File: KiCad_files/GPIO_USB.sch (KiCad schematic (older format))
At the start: 29 parts, among them J9 Conn_02x08_Odd_Even

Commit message: Cleanup + Update to KiCad 5.0 + DDR2
Updated to KiCad 5, which re-organized libraries, so corrected them to not need RASAC-rescue.lib.
Also cleaned up some stuff.
DDR4 has been removed and in place will be DDR2.
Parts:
- D10, D11, D12, D13, D14, D15, D16, D17, D18, D5, D6, D7, D8, D9: symbol LED_Small -> Device:LED_Small
- J9: symbol Conn_02x08_Odd_Even -> Connector_Generic:Conn_02x08_Odd_Even
- R74, R75, R76, R77, R78, R79, R80, R81, R82, R83, R84, R85, R86, R87: symbol R -> Device:R
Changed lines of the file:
@@
-EESchema Schematic File Version 2
-LIBS:power
-LIBS:device
-LIBS:switches
-LIBS:relays
-LIBS:motors
-LIBS:transistors
-LIBS:conn
-LIBS:linear
-LIBS:regul
-LIBS:74xx
-LIBS:cmos4000
-LIBS:adc-dac
-LIBS:memory
-LIBS:xilinx
-LIBS:microcontrollers
-LIBS:dsp
-LIBS:microchip
-LIBS:analog_switches
-LIBS:motorola
-LIBS:texas
-LIBS:intel
-LIBS:audio
-LIBS:interface
-LIBS:digital-audio
-LIBS:philips
-LIBS:display
-LIBS:cypress
-LIBS:siliconi
-LIBS:opto
-LIBS:atmel
-LIBS:contrib
-LIBS:valves
-LIBS:custom
-LIBS:Connector
+EESchema Schematic File Version 4
 LIBS:RASAC-cache
-EELAYER 25 0
+EELAYER 26 0
 EELAYER END
 $Descr A4 11693 8268
@@
 GPIO_4
 $Comp
-L Conn_02x08_Odd_Even J9
+L Connector_Generic:Conn_02x08_Odd_Even J9
 U 1 1 5C19A9DE
 P 3300 4100
@@
 $EndComp
 $Comp
-L R R74
+L Device:R R74
 U 1 1 5C19AB1A
 P 2400 4650
@@
 $EndComp
 $Comp
-L LED_Small D5
+L Device:LED_Small D5
 U 1 1 5C19AB43
 P 2400 4900
@@
 $EndComp
 $Comp
-L GND #PWR114
+L power:GND #PWR0114
 U 1 1 5C19AB94
 P 3100 5350
-F 0 "#PWR114" H 3100 5100 50  0001 C CNN
+F 0 "#PWR0114" H 3100 5100 50  0001 C CNN
 F 1 "GND" H 3100 5200 50  0001 C CNN
 F 2 "" H 3100 5350 50  0001 C CNN
@@
 $EndComp
 $Comp
-L R R75
+L Device:R R75
 U 1 1 5C19ACEE
 P 2500 5000
@@
 $EndComp
 $Comp
-L LED_Small D6
+L Device:LED_Small D6
 U 1 1 5C19ACF4
 P 2500 5250
@@
 $EndComp
 $Comp
-L LED_Small D7
+L Device:LED_Small D7
 U 1 1 5C19AF93
 P 2600 4900
@@
 $EndComp
 $Comp
-L R R77
+L Device:R R77
 U 1 1 5C19AF99
 P 2700 5000
@@
 $EndComp
 $Comp
-L LED_Small D8
+L Device:LED_Small D8
 U 1 1 5C19AF9F
 P 2700 5250
@@
 $EndComp
 $Comp
-L R R76
+L Device:R R76
 U 1 1 5C19AFBB
 P 2600 4650
@@
 $EndComp
 $Comp
-L LED_Small D9
+L Device:LED_Small D9
 U 1 1 5C19B20A
 P 2800 4900
@@
 $EndComp
 $Comp
-L R R79
+L Device:R R79
 U 1 1 5C19B210
 P 2900 5000
@@
 $EndComp
 $Comp
-L LED_Small D10
+L Device:LED_Small D10
 U 1 1 5C19B216
 P 2900 5250
@@
 $EndComp
 $Comp
-L R R78
+L Device:R R78
 U 1 1 5C19B21D
 P 2800 4650
@@
 $EndComp
 $Comp
-L LED_Small D11
+L Device:LED_Small D11
 U 1 1 5C19B32C
 P 3000 4900
@@
 $EndComp
 $Comp
-L R R80
+L Device:R R80
 U 1 1 5C19B33F
 P 3000 4650
@@
 $EndComp
 Wire Wire Line
-	2300 3800 3100 3800
-Wire Wire Line
-	2300 3900 3100 3900
-Wire Wire Line
-	2300 4000 3100 4000
-Wire Wire Line
-	3100 4100 2300 4100
-Wire Wire Line
-	2300 4200 3100 4200
-Wire Wire Line
-	3100 4300 2300 4300
-Wire Wire Line
-	2300 4400 3100 4400
-Wire Wire Line
-	3600 4400 4400 4400
-Wire Wire Line
-	3600 4300 4400 4300
-Wire Wire Line
-	3600 4200 4400 4200
-Wire Wire Line
-	3600 4100 4400 4100
-Wire Wire Line
-	4400 4000 3600 4000
-Wire Wire Line
-	3600 3900 4400 3900
-Wire Wire Line
-	4400 3800 3600 3800
+	2300 3800 2400 3800
+Wire Wire Line
+	2300 3900 2500 3900
+Wire Wire Line
+	2300 4000 2600 4000
+Wire Wire Line
+	3100 4100 2700 4100
+Wire Wire Line
+	2300 4200 2800 4200
+Wire Wire Line
+	3100 4300 2900 4300
+Wire Wire Line
+	2300 4400 3000 4400
+Wire Wire Line
+	3600 4400 3700 4400
+Wire Wire Line
+	3600 4300 3800 4300
+Wire Wire Line
+	3600 4200 3900 4200
+Wire Wire Line
+	3600 4100 4000 4100
+Wire Wire Line
+	4400 4000 4100 4000
+Wire Wire Line
+	3600 3900 4200 3900
+Wire Wire Line
+	4400 3800 4300 3800
 Wire Wire Line
 	2400 5000 2400 5350
 Wire Wire Line
-	2400 5350 3100 5350
+	2400 5350 2500 5350
 Wire Wire Line
 	2600 5350 2600 5000
@@
 Connection ~ 3000 5350
 $Comp
-L R R87
+L Device:R R87
 U 1 1 5C19B75D
 P 4300 4650
@@
 $EndComp
 $Comp
-L LED_Small D18
+L Device:LED_Small D18
 U 1 1 5C19B763
 P 4300 4900
@@
 $EndComp
 $Comp
-L R R86
+L Device:R R86
 U 1 1 5C19B769
 P 4200 5000
@@
 $EndComp
 $Comp
-L LED_Small D17
+L Device:LED_Small D17
 U 1 1 5C19B76F
 P 4200 5250
@@
 $EndComp
 $Comp
-L LED_Small D16
+L Device:LED_Small D16
 U 1 1 5C19B775
 P 4100 4900
@@
 $EndComp
 $Comp
-L R R84
+L Device:R R84
 U 1 1 5C19B77B
 P 4000 5000
@@
 $EndComp
 $Comp
-L LED_Small D15
+L Device:LED_Small D15
 U 1 1 5C19B781
 P 4000 5250
@@
 $EndComp
 $Comp
-L R R85
+L Device:R R85
 U 1 1 5C19B787
 P 4100 4650
@@
 $EndComp
 $Comp
-L LED_Small D14
+L Device:LED_Small D14
 U 1 1 5C19B78D
 P 3900 4900
@@
 $EndComp
 $Comp
-L R R82
+L Device:R R82
 U 1 1 5C19B793
 P 3800 5000
@@
 $EndComp
 $Comp
-L LED_Small D13
+L Device:LED_Small D13
 U 1 1 5C19B799
 P 3800 5250
@@
 $EndComp
 $Comp
-L R R83
+L Device:R R83
 U 1 1 5C19B79F
 P 3900 4650
@@
 $EndComp
 $Comp
-L LED_Small D12
+L Device:LED_Small D12
 U 1 1 5C19B7A5
 P 3700 4900
@@
 $EndComp
 $Comp
-L R R81
+L Device:R R81
 U 1 1 5C19B7AB
 P 3700 4650
@@
 	4300 5350 4300 5000
 Wire Wire Line
-	3600 5350 4300 5350
+	3600 5350 3700 5350
 Wire Wire Line
 	4100 5350 4100 5000
@@
 Connection ~ 3700 5350
 $Comp
-L GND #PWR115
+L power:GND #PWR0115
 U 1 1 5C19BABD
 P 3600 5350
-F 0 "#PWR115" H 3600 5100 50  0001 C CNN
+F 0 "#PWR0115" H 3600 5100 50  0001 C CNN
 F 1 "GND" H 3600 5200 50  0001 C CNN
 F 2 "" H 3600 5350 50  0001 C CNN
@@
 Text Notes 7050 4350 0    60   ~ 0
 USB Controller?
+Wire Wire Line
+	2600 5350 2700 5350
+Wire Wire Line
+	2500 5350 2600 5350
+Wire Wire Line
+	2700 5350 2800 5350
+Wire Wire Line
+	2900 5350 3000 5350
+Wire Wire Line
+	2800 5350 2900 5350
+Wire Wire Line
+	3000 5350 3100 5350
+Wire Wire Line
+	4100 5350 4200 5350
+Wire Wire Line
+	4200 5350 4300 5350
+Wire Wire Line
+	4000 5350 4100 5350
+Wire Wire Line
+	3800 5350 3900 5350
+Wire Wire Line
+	3900 5350 4000 5350
+Wire Wire Line
+	3700 5350 3800 5350
+Wire Wire Line
+	2400 3800 3100 3800
+Wire Wire Line
+	2500 3900 3100 3900
+Wire Wire Line
+	2600 4000 3100 4000
+Wire Wire Line
+	2700 4100 2300 4100
+Wire Wire Line
+	2800 4200 3100 4200
+Wire Wire Line
+	2900 4300 2300 4300
+Wire Wire Line
+	3000 4400 3100 4400
+Wire Wire Line
+	3700 4400 4400 4400
+Wire Wire Line
+	3800 4300 4400 4300
+Wire Wire Line
+	3900 4200 4400 4200
+Wire Wire Line
+	4000 4100 4400 4100
+Wire Wire Line
+	4100 4000 3600 4000
+Wire Wire Line
+	4200 3900 4400 3900
+Wire Wire Line
+	4300 3800 3600 3800
 $EndSCHEMATC

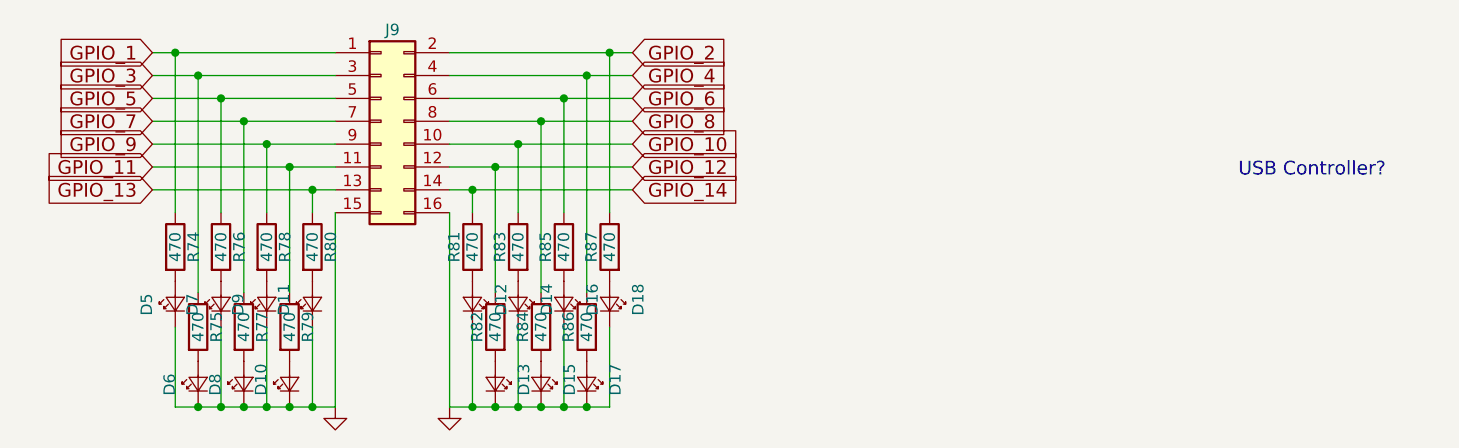
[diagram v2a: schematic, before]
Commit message: Finished HDMI. Added I2C
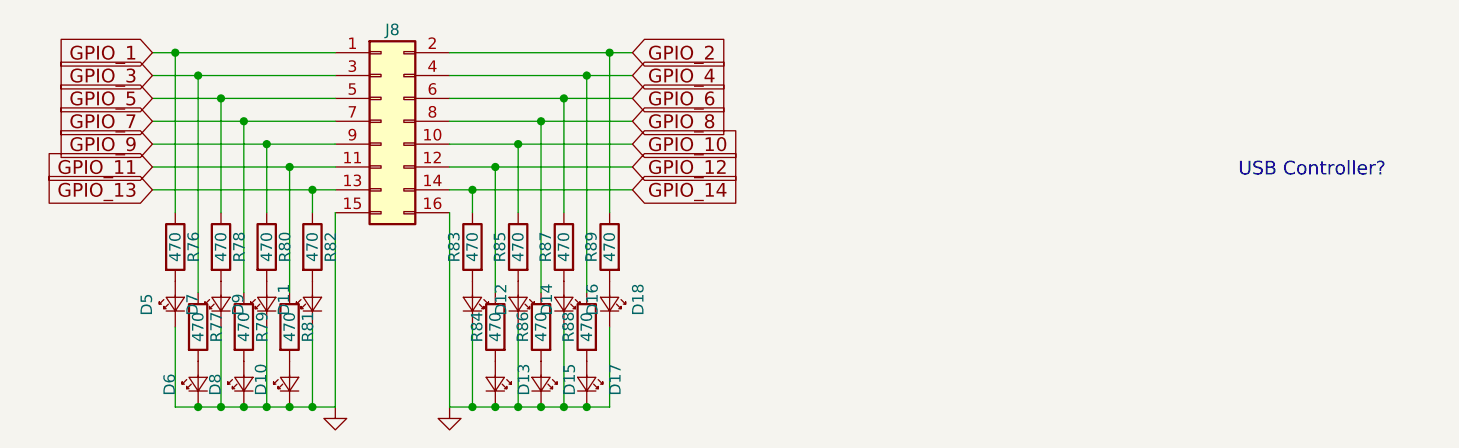
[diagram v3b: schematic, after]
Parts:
- renumbered J9 to J8, R74 to R76, R75 to R77, R76 to R78, R77 to R79, R78 to R80, R79 to R81, R80 to R82, R81 to R83, R82 to R84, R83 to R85, R84 to R86, R85 to R87, R86 to R88, R87 to R89
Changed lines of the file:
@@
 GPIO_4
 $Comp
-L Connector_Generic:Conn_02x08_Odd_Even J9
+L Connector_Generic:Conn_02x08_Odd_Even J8
 U 1 1 5C19A9DE
 P 3300 4100
-F 0 "J9" H 3350 4500 50  0000 C CNN
+F 0 "J8" H 3350 4500 50  0000 C CNN
 F 1 "Conn_02x08_Odd_Even" H 3350 3600 50  0001 C CNN
 F 2 "" H 3300 4100 50  0001 C CNN
@@
 $EndComp
 $Comp
-L Device:R R74
+L Device:R R76
 U 1 1 5C19AB1A
 P 2400 4650
-F 0 "R74" V 2480 4650 50  0000 C CNN
+F 0 "R76" V 2480 4650 50  0000 C CNN
 F 1 "470" V 2400 4650 50  0000 C CNN
 F 2 "" V 2330 4650 50  0001 C CNN
@@
 $EndComp
 $Comp
-L power:GND #PWR0114
+L power:GND #PWR0122
 U 1 1 5C19AB94
 P 3100 5350
-F 0 "#PWR0114" H 3100 5100 50  0001 C CNN
+F 0 "#PWR0122" H 3100 5100 50  0001 C CNN
 F 1 "GND" H 3100 5200 50  0001 C CNN
 F 2 "" H 3100 5350 50  0001 C CNN
@@
 $EndComp
 $Comp
-L Device:R R75
+L Device:R R77
 U 1 1 5C19ACEE
 P 2500 5000
-F 0 "R75" V 2580 5000 50  0000 C CNN
+F 0 "R77" V 2580 5000 50  0000 C CNN
 F 1 "470" V 2500 5000 50  0000 C CNN
 F 2 "" V 2430 5000 50  0001 C CNN
@@
 $EndComp
 $Comp
-L Device:R R77
+L Device:R R79
 U 1 1 5C19AF99
 P 2700 5000
-F 0 "R77" V 2780 5000 50  0000 C CNN
+F 0 "R79" V 2780 5000 50  0000 C CNN
 F 1 "470" V 2700 5000 50  0000 C CNN
 F 2 "" V 2630 5000 50  0001 C CNN
@@
 $EndComp
 $Comp
-L Device:R R76
+L Device:R R78
 U 1 1 5C19AFBB
 P 2600 4650
-F 0 "R76" V 2680 4650 50  0000 C CNN
+F 0 "R78" V 2680 4650 50  0000 C CNN
 F 1 "470" V 2600 4650 50  0000 C CNN
 F 2 "" V 2530 4650 50  0001 C CNN
@@
 $EndComp
 $Comp
-L Device:R R79
+L Device:R R81
 U 1 1 5C19B210
 P 2900 5000
-F 0 "R79" V 2980 5000 50  0000 C CNN
+F 0 "R81" V 2980 5000 50  0000 C CNN
 F 1 "470" V 2900 5000 50  0000 C CNN
 F 2 "" V 2830 5000 50  0001 C CNN
@@
 $EndComp
 $Comp
-L Device:R R78
+L Device:R R80
 U 1 1 5C19B21D
 P 2800 4650
-F 0 "R78" V 2880 4650 50  0000 C CNN
+F 0 "R80" V 2880 4650 50  0000 C CNN
 F 1 "470" V 2800 4650 50  0000 C CNN
 F 2 "" V 2730 4650 50  0001 C CNN
@@
 $EndComp
 $Comp
-L Device:R R80
+L Device:R R82
 U 1 1 5C19B33F
 P 3000 4650
-F 0 "R80" V 3080 4650 50  0000 C CNN
+F 0 "R82" V 3080 4650 50  0000 C CNN
 F 1 "470" V 3000 4650 50  0000 C CNN
 F 2 "" V 2930 4650 50  0001 C CNN
@@
 Connection ~ 3000 5350
 $Comp
-L Device:R R87
+L Device:R R89
 U 1 1 5C19B75D
 P 4300 4650
-F 0 "R87" V 4380 4650 50  0000 C CNN
+F 0 "R89" V 4380 4650 50  0000 C CNN
 F 1 "470" V 4300 4650 50  0000 C CNN
 F 2 "" V 4230 4650 50  0001 C CNN
@@
 $EndComp
 $Comp
-L Device:R R86
+L Device:R R88
 U 1 1 5C19B769
 P 4200 5000
-F 0 "R86" V 4280 5000 50  0000 C CNN
+F 0 "R88" V 4280 5000 50  0000 C CNN
 F 1 "470" V 4200 5000 50  0000 C CNN
 F 2 "" V 4130 5000 50  0001 C CNN
@@
 $EndComp
 $Comp
-L Device:R R84
+L Device:R R86
 U 1 1 5C19B77B
 P 4000 5000
-F 0 "R84" V 4080 5000 50  0000 C CNN
+F 0 "R86" V 4080 5000 50  0000 C CNN
 F 1 "470" V 4000 5000 50  0000 C CNN
 F 2 "" V 3930 5000 50  0001 C CNN
@@
 $EndComp
 $Comp
-L Device:R R85
+L Device:R R87
 U 1 1 5C19B787
 P 4100 4650
-F 0 "R85" V 4180 4650 50  0000 C CNN
+F 0 "R87" V 4180 4650 50  0000 C CNN
 F 1 "470" V 4100 4650 50  0000 C CNN
 F 2 "" V 4030 4650 50  0001 C CNN
@@
 $EndComp
 $Comp
-L Device:R R82
+L Device:R R84
 U 1 1 5C19B793
 P 3800 5000
-F 0 "R82" V 3880 5000 50  0000 C CNN
+F 0 "R84" V 3880 5000 50  0000 C CNN
 F 1 "470" V 3800 5000 50  0000 C CNN
 F 2 "" V 3730 5000 50  0001 C CNN
@@
 $EndComp
 $Comp
-L Device:R R83
+L Device:R R85
 U 1 1 5C19B79F
 P 3900 4650
-F 0 "R83" V 3980 4650 50  0000 C CNN
+F 0 "R85" V 3980 4650 50  0000 C CNN
 F 1 "470" V 3900 4650 50  0000 C CNN
 F 2 "" V 3830 4650 50  0001 C CNN
@@
 $EndComp
 $Comp
-L Device:R R81
+L Device:R R83
 U 1 1 5C19B7AB
 P 3700 4650
-F 0 "R81" V 3780 4650 50  0000 C CNN
+F 0 "R83" V 3780 4650 50  0000 C CNN
 F 1 "470" V 3700 4650 50  0000 C CNN
 F 2 "" V 3630 4650 50  0001 C CNN
@@
 Connection ~ 3700 5350
 $Comp
-L power:GND #PWR0115
+L power:GND #PWR0123
 U 1 1 5C19BABD
 P 3600 5350
-F 0 "#PWR0115" H 3600 5100 50  0001 C CNN
+F 0 "#PWR0123" H 3600 5100 50  0001 C CNN
 F 1 "GND" H 3600 5200 50  0001 C CNN
 F 2 "" H 3600 5350 50  0001 C CNN
